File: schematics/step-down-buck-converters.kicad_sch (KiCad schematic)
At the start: 16 parts, among them U1 TPS54308, U3 TPS62203DBVTG4

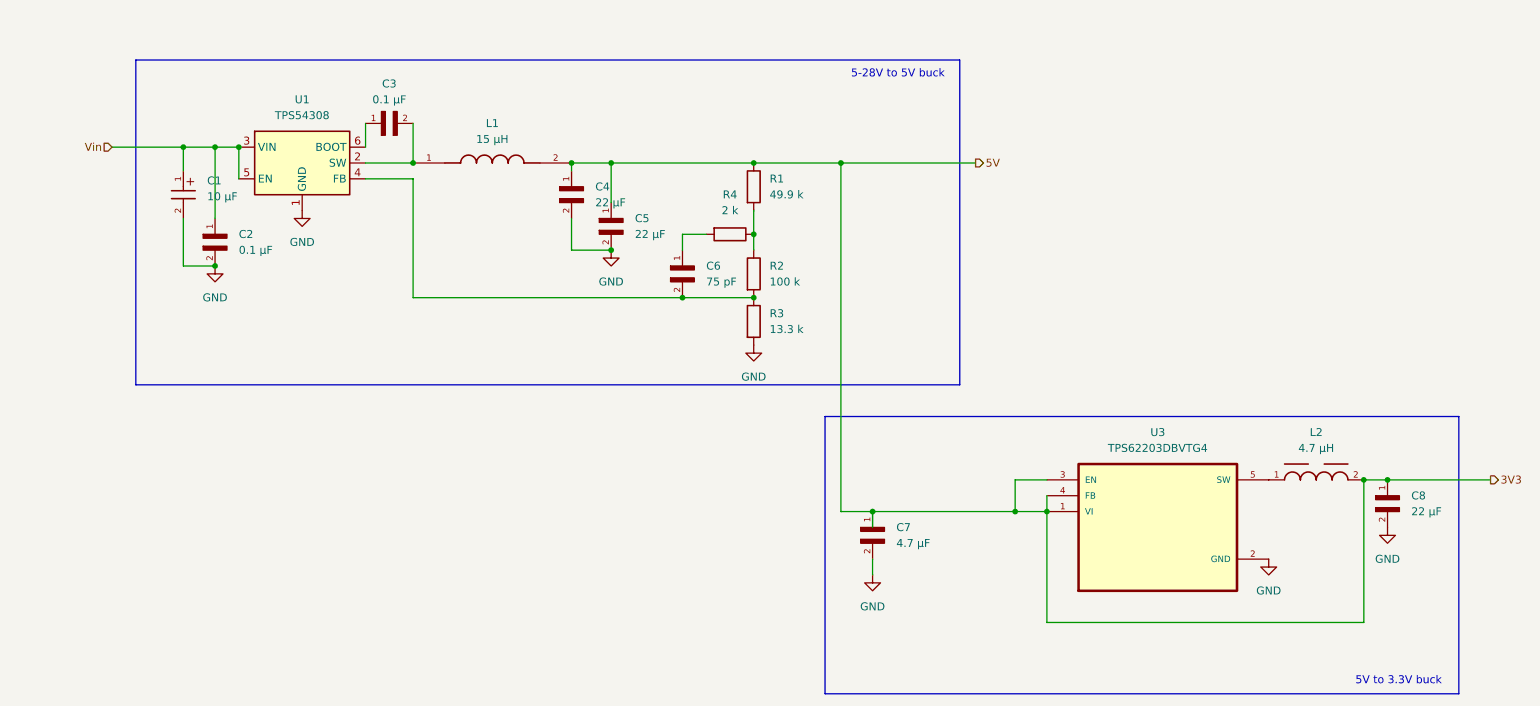
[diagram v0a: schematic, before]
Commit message: 12-to-5V buck review
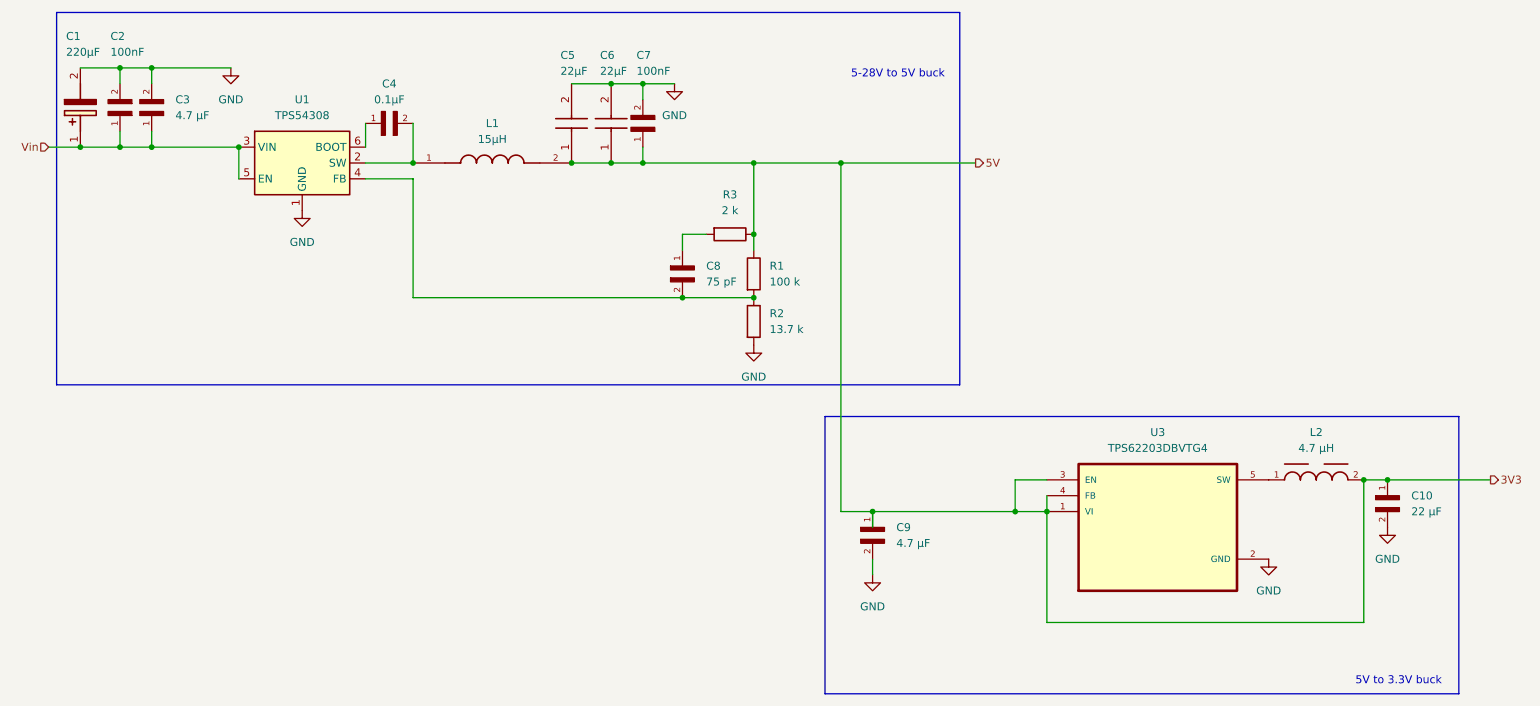
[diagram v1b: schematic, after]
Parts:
- removed C1: 10 µF, WCAP-ATG8_5X11:WCAP-ATG8_5X11_DXL_, symbol WCAP-ATG8_5X11:WCAP-ATG8_5X11
- removed C2: 0.1 µF, MBJCG168BB7104KTPA18:CAPC1608X100N, symbol MBJCG168BB7104KTPA18:MBJCG168BB7104KTPA18
- removed C4, C5: 22 µF, MLASG32MSB5226MPNA01:CAPC3225X270N, symbol MLASG32MSB5226MPNA01:MLASG32MSB5226MPNA01
- removed R1: 49.9 k, Resistor_SMD:R_0603_1608Metric, symbol Device:R
- added C1: 220µF, EEU-FC1H221S:CAPPRD500W65D1250H1600, symbol EEU-FC1H221S:EEU-FC1H221S
- added C2, C7: 100nF, 08055C104KAT4A:CAPC2012X94N, symbol 08055C104KAT4A:08055C104KAT4A
- added C3: 4.7 µF, MCASL21GBC7475MTCA01:CAPC2012X145N, symbol MCASL21GBC7475MTCA01:MCASL21GBC7475MTCA01
- added C5, C6: 22µF, MBAST32MSB7226KPNA18:CAPC3225X270N, symbol MBAST32MSB7226KPNA18:MBAST32MSB7226KPNA18
- C4: renamed from C3; value 0.1 µF -> 0.1µF
- L1: value 15 µH -> 15µH
- R2: renamed from R3; value 13.3 k -> 13.7 k
- renumbered C8 to C10, C6 to C8, C7 to C9, R2 to R1, R4 to R3
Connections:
- net 3V3: now also R1.1, R3.1, C5.1, C6.1, C7.1
- net GND: now also C1.2 (-), C2.2, C3.2, C5.2, C6.2, C7.2
- net Vin: now also C1.1 (+), C2.1, C3.1

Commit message: Replaced L1 with lower resistance one
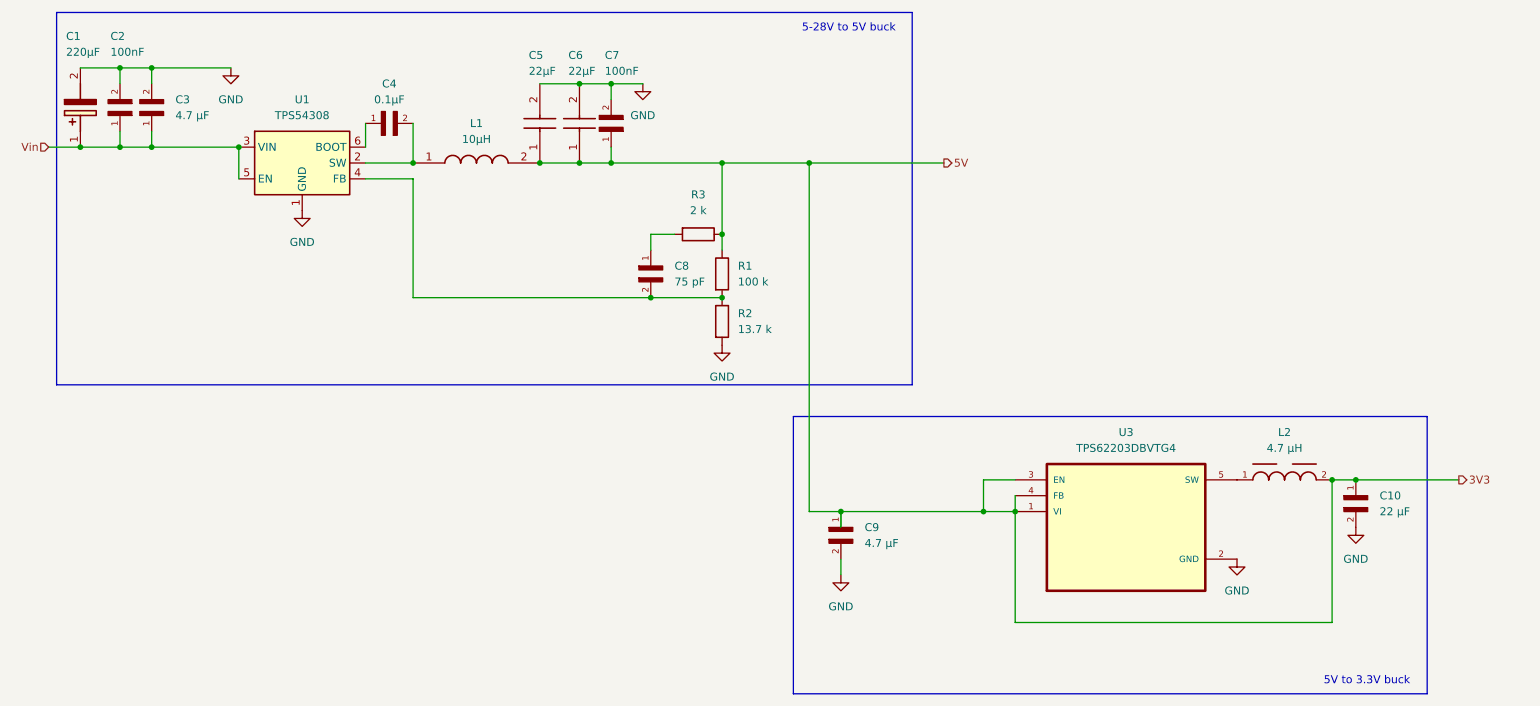
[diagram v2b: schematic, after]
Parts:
- removed L1: 15µH, ASPI-0804T-150M-T:IND_ASPI-0804T-150M-T, symbol ASPI-0804T-150M-T:ASPI-0804T-150M-T
- added L1: 10µH, DR125-100-R:INDPM125125X600N, symbol DR125-100-R:DR125-100-R
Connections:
- net 3V3: now also L1.2
- net at C4.2, U1.2 (SW): now also L1.1
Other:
- moved on the sheet: C10, C5, C6, C7, C8, C9, L2, R1, R2, R3, U3
